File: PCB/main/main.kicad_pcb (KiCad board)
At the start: 2 copper layers, 121.9 x 91.4 mm, 53 parts, among them IC1 LM358DT, IC2 LM358DT, IC3 AT24C256C-SSHL-T, J1 Conn_01x33_Female, J2 Conn_01x33_Female, J3 Conn_01x33_Female, J4 Conn_01x33_Female, J5 47346-0001, J5 USB_B_Micro, Q1 IRF9540NPbF, U1 MCP73831-2-OT, U2 FT232RL, U3 MCP1700-3302E_TO92

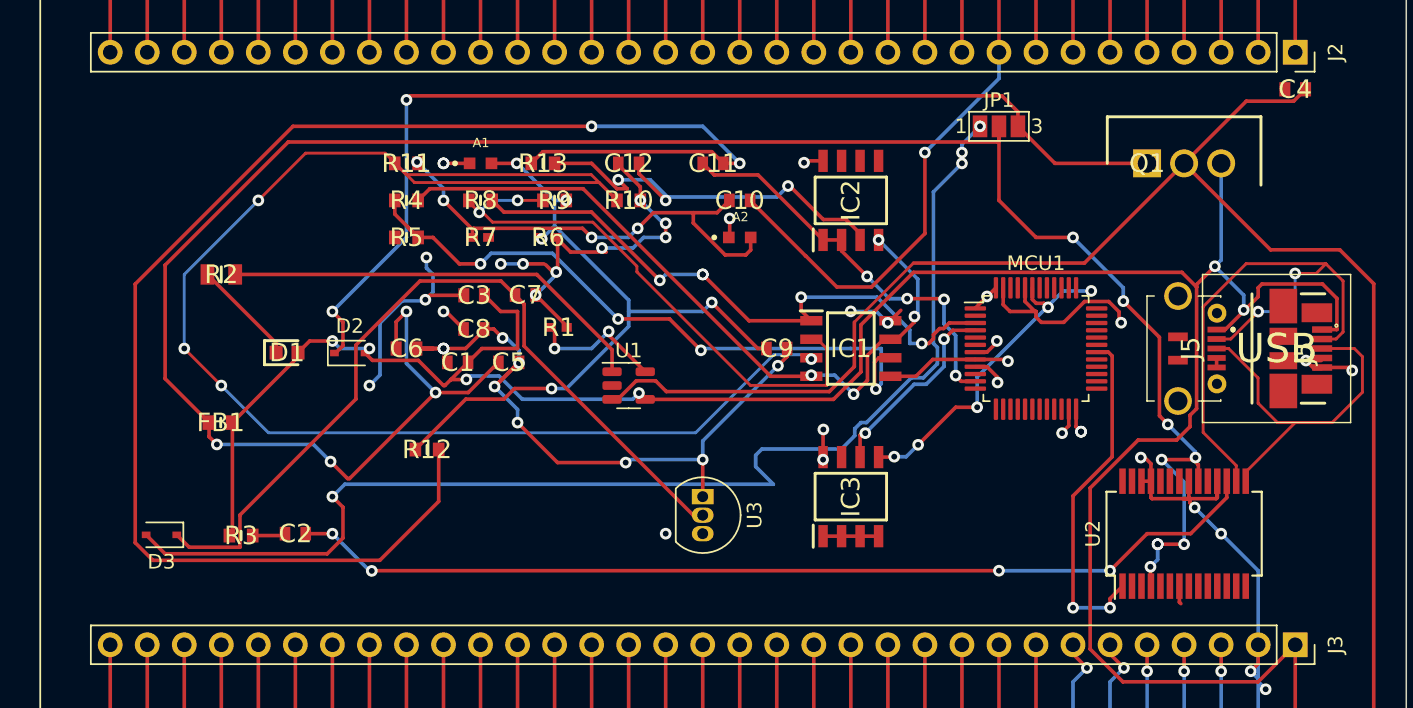
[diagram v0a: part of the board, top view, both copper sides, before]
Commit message: added more test points
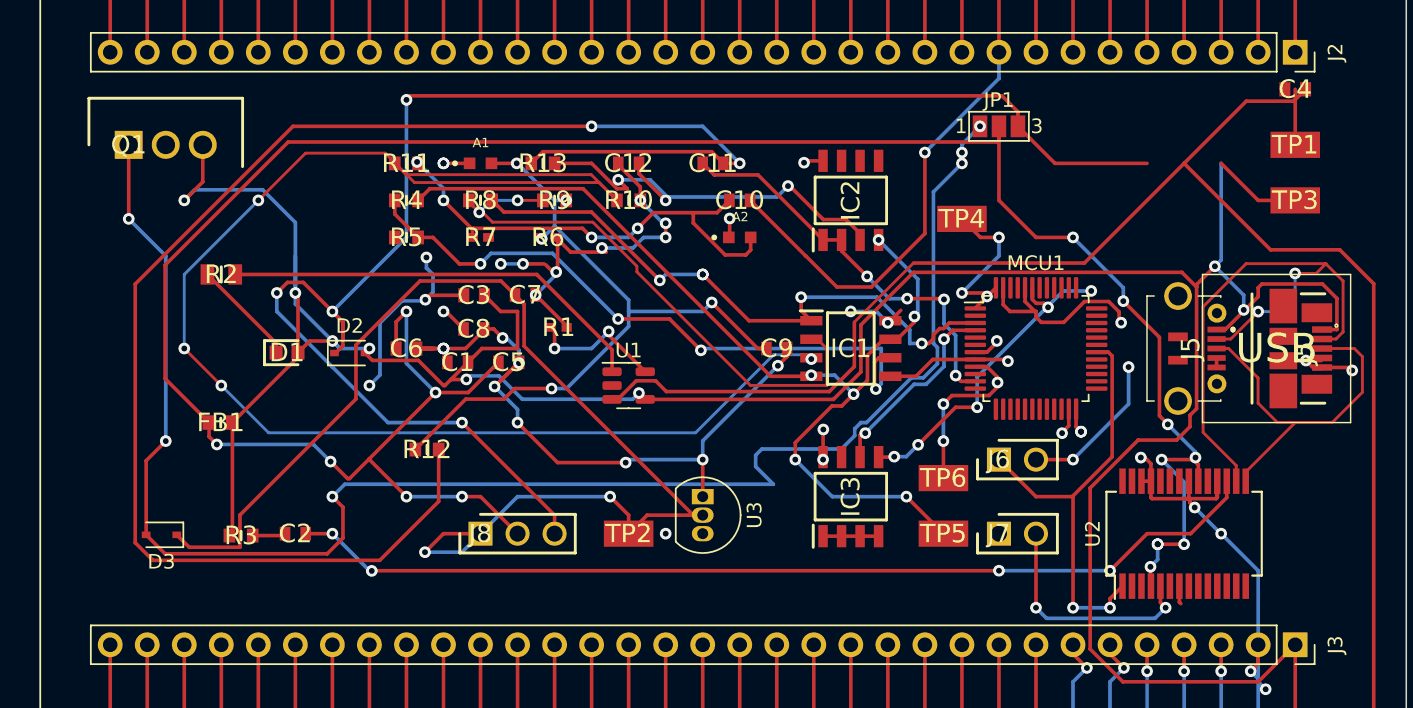
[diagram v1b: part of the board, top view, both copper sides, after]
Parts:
- added J6: PZ254V-11-02P, SamacSys_Parts:HDRV2W64P0X254_1X2_508X250X873P, F.Cu at (160.0, 104.1)
- added J7: PZ254V-11-02P, SamacSys_Parts:HDRV2W64P0X254_1X2_508X250X873P, F.Cu at (160.0, 109.2)
- added J8: MTP125-1103S1, SamacSys_Parts:HDRV3W64P0X254_1X3_762X250X885P, F.Cu at (124.5, 109.2)
- added TP1: 5017, SamacSys_Parts:5017, F.Cu at (180.3, 82.5)
- added TP2: 5017, SamacSys_Parts:5017, F.Cu at (134.6, 109.2)
- added TP3: 5017, SamacSys_Parts:5017, F.Cu at (180.3, 86.4)
- added TP4: 5017, SamacSys_Parts:5017, F.Cu at (157.5, 87.6)
- added TP5: 5017, SamacSys_Parts:5017, F.Cu at (156.2, 109.2)
- added TP6: 5017, SamacSys_Parts:5017, F.Cu at (156.2, 105.4)
- moved Q1 69.9 mm to (100.3, 82.5)
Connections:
- D3 pad 1: Net-(C7-Pad1) -> Net-(D2-Pad1)
- Q1 pad 1: Net-(D2-Pad1) -> Net-(D3-Pad2)
- U2 pad 1: USART1_TX -> Net-(J6-Pad1)
- U2 pad 5: USATR1_RX -> Net-(J7-Pad2)
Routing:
- net +5V: track 177.9 -> 213.8 mm, vias 6 -> 8
- net Net-(D2-Pad1): track 73.5 -> 107.9 mm, vias 2 -> 4
- net Net-(J6-Pad1): track 0.00 -> 30.1 mm, vias 0 -> 2
- net Net-(D3-Pad2): track 83.8 -> 112.1 mm, vias 4 -> 6
- net Net-(C7-Pad1): track 55.8 -> 83.1 mm, vias 0 -> 2
- net +3v3: track 20.9 -> 40.1 mm, vias 15 -> 19
- net -3v3: track 50.1 -> 68.9 mm, vias 4 -> 6
- net Net-(J7-Pad2): track 0.00 -> 16.2 mm, vias 0 -> 2
- net USART1_TX: track 23.9 -> 10.7 mm
- net VCC: track 153.4 -> 165.8 mm, vias 13 -> 15
- net Net-(BT1-Pad1): track 216.3 -> 220.1 mm

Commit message: pcb update
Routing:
- net Net-(BT1-Pad1): track 220.1 -> 272.0 mm, vias 0 -> 4
- net Net-(C7-Pad1): track 83.1 -> 48.1 mm
- net Net-(D2-Pad1): track 107.9 -> 124.0 mm, vias 4 -> 7
- net Net-(J6-Pad1): track 30.1 -> 17.3 mm
- net IN2-: track 45.9 -> 57.9 mm
- net GND: track 233.3 -> 244.3 mm, vias 31 -> 32
- net USART1_TX: track 10.7 -> 13.3 mm

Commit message: gerber files and dat
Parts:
- added C13: CC0603KRX7R9BB104, SamacSys_Parts:CAPC1608X90N, F.Cu at (99.1, 91.4)
- added J9: PZ254V-11-02P, SamacSys_Parts_Power:HDRV2W64P0X254_1X2_508X250X873P, F.Cu at (167.6, 81.3)
- added TP5: 5017, SamacSys_Parts_Power:5017, F.Cu at (144.8, 91.4)
- added TP6: 5017, SamacSys_Parts_Power:5017, B.Cu at (147.3, 81.3)
- added TP7: 5017, SamacSys_Parts_Power:5017, B.Cu at (162.6, 86.4)
- renumbered D3 to D2, D2 to D3, TP3 to TP1, TP1 to TP2, TP2 to TP3, TP5 to TP8, TP6 to TP9
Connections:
- D2 pad 2: Net-(D3-Pad2) -> (no net)
- MCU1 pad 7: +3v3 -> Net-(C13-Pad1)
- Q1 pad 1: Net-(D3-Pad2) -> Net-(D2-Pad2)
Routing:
- net Net-(D3-Pad2): track 112.1 -> 0.00 mm, vias 6 -> 0
- net Net-(D2-Pad2): track 0.00 -> 109.2 mm, vias 0 -> 4
- net GND: track 244.3 -> 295.9 mm, vias 32 -> 29
- net Vdiff: track 42.1 -> 73.5 mm
- net +3v3: track 40.1 -> 67.4 mm, vias 19 -> 17
- net Net-(C13-Pad1): track 0.00 -> 19.8 mm, vias 0 -> 2
- net Vout2: track 32.3 -> 43.7 mm, vias 4 -> 7
- net Net-(D2-Pad1): track 124.0 -> 114.5 mm
- net Vout1: track 47.5 -> 56.5 mm
- net Net-(BT1-Pad1): track 272.0 -> 271.2 mm
- net +5V: vias 8 -> 10

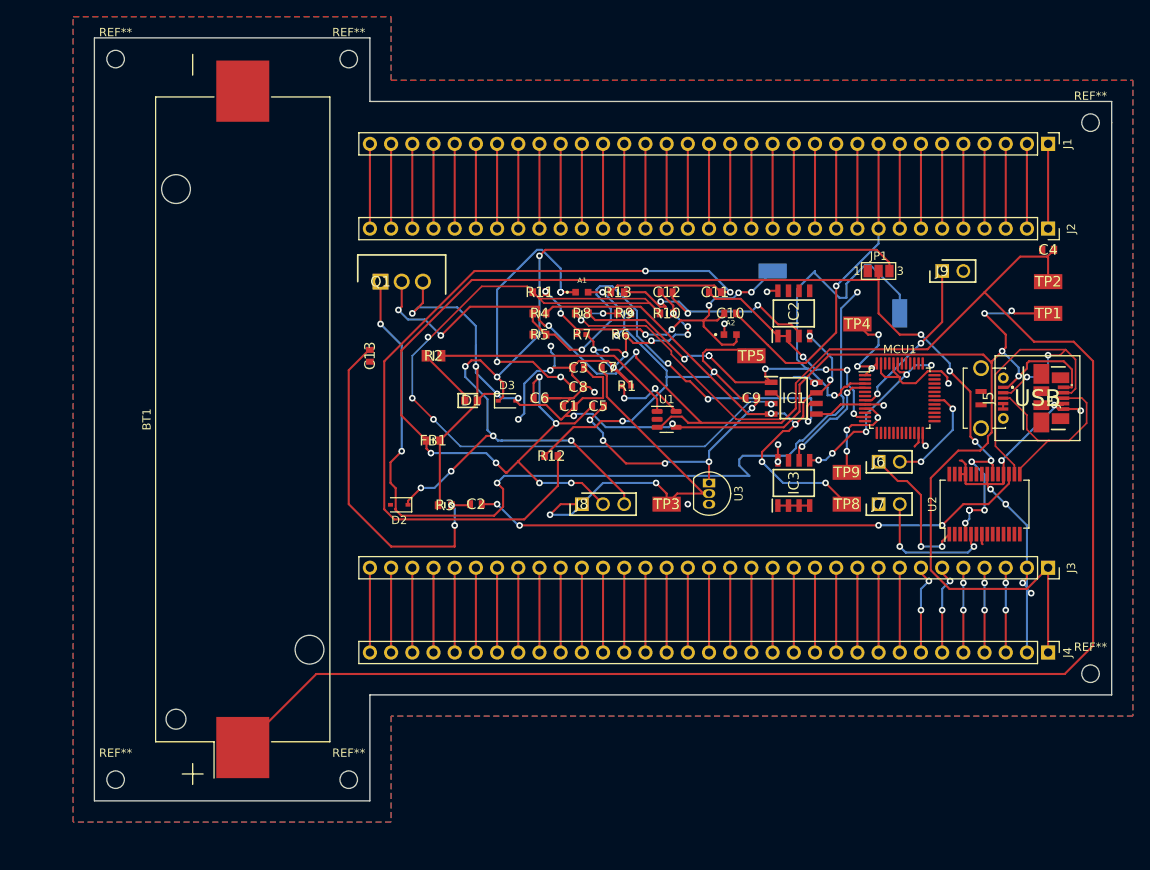
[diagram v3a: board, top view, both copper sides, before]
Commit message: modified power schematic
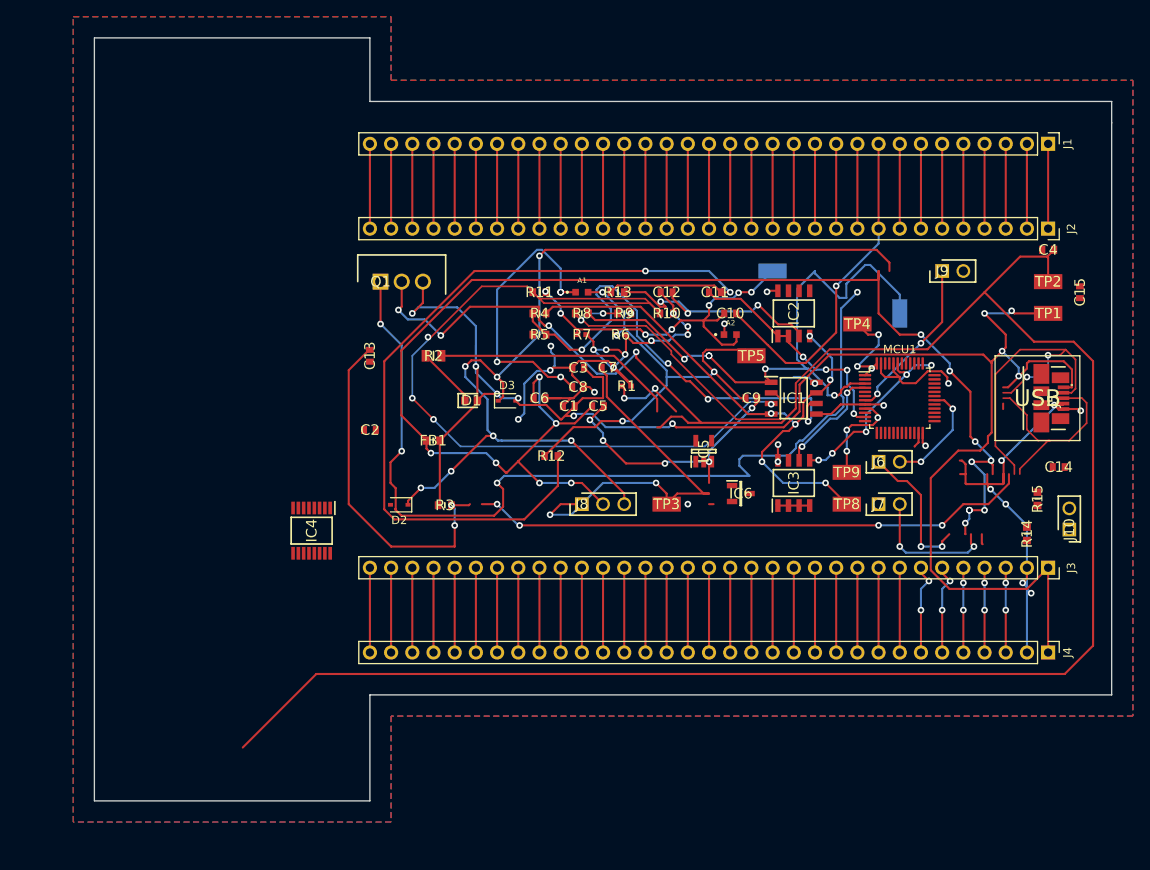
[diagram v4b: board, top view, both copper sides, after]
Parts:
- removed BT1: 3.7V, Battery:BatteryHolder_Keystone_1042_1x18650
- removed the J5 at (170.2, 96.5)
- removed JP1: Jumper_3_Open, Jumper:SolderJumper-3_P1.3mm_Open_Pad1.0x1.5mm_NumberLabels
- removed REF** (x6): MountingHole_2.1mm, MountingHole:MountingHole_2.1mm
- removed U1: MCP73831-2-OT, Package_TO_SOT_SMD:SOT-23-5
- removed U2: FT232RL, Package_SO:SSOP-28_5.3x10.2mm_P0.65mm
- removed U3: MCP1700-3302E_TO92, Package_TO_SOT_THT:TO-92_Inline
- added C14: CL10C470JB8NNNC, CAP1UF:CAPC1608X90N, F.Cu at (181.6, 104.8)
- added C15: CL10C470JB8NNNC, CAP1UF:CAPC1608X90N, F.Cu at (184.2, 83.8)
- added IC4: FT230XS-R, SamacSys_Parts:SOP64P599X175-16N, F.Cu at (92.1, 112.4)
- added IC5: MCP73831T-2ACI_OT, SamacSys_Parts:SOT95P270X145-5N, F.Cu at (139.1, 102.9)
- added IC6: MCP1700T-3302E_TT, SamacSys_Parts:SOT95P237X112-3N, F.Cu at (143.5, 108.0)
- added J10: PZ254V-11-02P, SamacSys_Parts:HDRV2W64P0X254_1X2_508X250X873P, F.Cu at (182.9, 112.3)
- added R14: 0603WAF270JT5E, R10K:RESC1608X55N, F.Cu at (177.8, 112.8)
- added R15: 0603WAF270JT5E, R10K:RESC1608X55N, F.Cu at (179.1, 108.6)
- C13: footprint SamacSys_Parts:CAPC1608X90N -> CAP1UF:CAPC1608X90N
- C2: value 100nF -> CC0603KRX7R9BB104; footprint SamacSys_Parts:CAPC1608X90N -> CAP1UF:CAPC1608X90N
- J9: footprint SamacSys_Parts_Power:HDRV2W64P0X254_1X2_508X250X873P -> SamacSys_Parts:HDRV2W64P0X254_1X2_508X250X873P
- TP5, TP6, TP7: footprint SamacSys_Parts_Power:5017 -> SamacSys_Parts:5017
- moved C2 15.5 mm to (99.1, 100.3)
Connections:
- C13 pad 1: (no net) -> Net-(C13-Pad1)
- C2 pad 1: GND -> /Power/3V3
- C2 pad 2: Net-(C2-Pad2) -> GND
- D2 pad 2: (no net) -> Net-(D2-Pad2)
- J6 pad 1: Net-(J6-Pad1) -> /Power/TXD
- J7 pad 2: Net-(J7-Pad2) -> /Power/RXD
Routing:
- net (no net): track 0.00 -> 68.1 mm, vias 0 -> 4
- net Net-(C2-Pad2): track 67.4 -> 0.00 mm, vias 4 -> 0
- net Net-(J6-Pad1): track 17.3 -> 0.00 mm, vias 2 -> 0
- net /Power/TXD: track 0.00 -> 17.3 mm, vias 0 -> 2
- net Net-(J7-Pad2): track 16.2 -> 0.00 mm, vias 2 -> 0
- net /Power/RXD: track 0.00 -> 16.2 mm, vias 0 -> 2
- net Earth: track 0.65 -> 0.00 mm

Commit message: new PCB
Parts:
- removed MCU1: STM32F030C8Tx, Package_QFP:LQFP-48_7x7mm_P0.5mm
- C13, C14, C15, C2: footprint CAP1UF:CAPC1608X90N -> SamacSys_Parts:CAPC1608X90N
- IC4: footprint SamacSys_Parts:SOP64P599X175-16N -> SamacSys_Parts_Power:SOP64P599X175-16N
- IC5: footprint SamacSys_Parts:SOT95P270X145-5N -> SamacSys_Parts_Power:SOT95P270X145-5N
- IC6: footprint SamacSys_Parts:SOT95P237X112-3N -> SamacSys_Parts_Power:SOT95P237X112-3N
- J10, J6, J7, J9: footprint SamacSys_Parts:HDRV2W64P0X254_1X2_508X250X873P -> SamacSys_Parts_Power:HDRV2W64P0X254_1X2_508X250X873P
- J5: footprint SamacSys_Parts_Power:47346-0001 -> SamacSys_Parts_Microcontroller:47346-0001
- J8: footprint SamacSys_Parts:HDRV3W64P0X254_1X3_762X250X885P -> SamacSys_Parts_Power:HDRV3W64P0X254_1X3_762X250X885P
- R14, R15: footprint R10K:RESC1608X55N -> SamacSys_Parts:RESC1608X55N
- TP1, TP2, TP3, TP4, TP5, TP8, TP9: footprint SamacSys_Parts:5017 -> SamacSys_Parts_Power:5017
- TP6, TP7: footprint SamacSys_Parts:5017 -> SamacSys_Parts_Power:5017; moved to F.Cu
- moved J10 82.4 mm to (101.6, 98.7), turned to 180 degrees
- moved R4 70.6 mm to (179.6, 123.2), turned to 90 degrees
- moved C13 67.1 mm to (164.1, 107.7), turned to 0 degrees
- moved TP6 65.3 mm to (105.0, 131.0), turned to 0 degrees
- moved R7 63.4 mm to (172.6, 130.2), turned to 180 degrees
- moved R11 63.4 mm to (172.6, 118.2)
- moved J6 61.7 mm to (98.6, 109.7)
- moved R5 58.4 mm to (161.7, 129.2)
- moved A2 58.0 mm to (99.6, 128.2)
- moved TP1 55.6 mm to (131.1, 112.2), turned to -90 degrees
- moved Q1 54.7 mm to (131.2, 127.7), turned to 180 degrees
- moved R9 54.0 mm to (167.1, 125.2)
- moved TP2 52.4 mm to (131.0, 100.3)
- moved C4 52.0 mm to (140.1, 111.7), turned to -90 degrees
- moved C15 49.1 mm to (145.6, 114.2), turned to 90 degrees
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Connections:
- net Net-(C13-Pad1) renamed /microcontroller_interfacing/NRST
- net USATR1_RX renamed /Power/PA10
- IC3 pad 5: /microcontroller_interfacing/SDA_P43 -> /microcontroller_interfacing/PB7
- IC3 pad 6: /microcontroller_interfacing/SCL_P4 -> /microcontroller_interfacing/PC15
- J6 pad 2: USART1_TX -> /Power/PA9
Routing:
- net Net-(C4-Pad2): track 271.2 -> 79.9 mm, vias 4 -> 2
- net Net-(D2-Pad2): track 109.2 -> 8.55 mm, vias 4 -> 0
- net VCC: track 165.8 -> 75.1 mm, vias 15 -> 0
- net Net-(C11-Pad2): track 106.2 -> 18.9 mm, vias 2 -> 0
- net IN1+: track 103.8 -> 17.8 mm, vias 4 -> 3
- net Net-(D2-Pad1): track 114.5 -> 54.4 mm, vias 7 -> 4
- net Net-(IC4-Pad8): track 0.00 -> 49.2 mm, vias 0 -> 2
- net Vdiff: track 73.5 -> 25.6 mm, vias 5 -> 2
- net GND: track 295.9 -> 248.9 mm, vias 29 -> 40
- net Vout2: track 43.7 -> 89.0 mm, vias 7 -> 2
- net +3v3: track 67.4 -> 110.4 mm, vias 17 -> 8
- net Vout1: track 56.5 -> 94.9 mm, vias 5 -> 6
- net (no net): track 68.1 -> 31.6 mm, vias 4 -> 7
- net +5V: track 213.8 -> 180.9 mm
- net Net-(IC4-Pad9): track 0.00 -> 31.6 mm, vias 0 -> 4
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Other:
- board size 121.9 x 91.4 mm -> 97 x 73 mm

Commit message: generated Gerbers
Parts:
- added REF**: MountingHole_2.1mm, MountingHole:MountingHole_2.1mm, F.Cu at (185.9, 82.8)
- added REF**: MountingHole_2.1mm, MountingHole:MountingHole_2.1mm, F.Cu at (186.4, 146.8)
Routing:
- net GND: track 248.9 -> 244.5 mm
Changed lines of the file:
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@@
       (layerselection 0x00010fc_ffffffff)
       (disableapertmacros false)
-      (usegerberextensions false)
-      (usegerberattributes true)
-      (usegerberadvancedattributes true)
-      (creategerberjobfile true)
+      (usegerberextensions true)
+      (usegerberattributes false)
+      (usegerberadvancedattributes false)
+      (creategerberjobfile false)
       (svguseinch false)
       (svgprecision 6)
@@
       (psa4output false)
       (plotreference true)
-      (plotvalue true)
+      (plotvalue false)
       (plotinvisibletext false)
       (sketchpadsonfab false)
-      (subtractmaskfromsilk false)
+      (subtractmaskfromsilk true)
       (outputformat 1)
       (mirror false)
-      (drillshape 1)
+      (drillshape 0)
       (scaleselection 1)
-      (outputdirectory "")
+      (outputdirectory "Gerbers/")
     )
   )
@@
     )
   )
+  (footprint "MountingHole:MountingHole_2.1mm" (layer "F.Cu")
+    (at 185.928 82.804)
+    (descr "Mounting Hole 2.1mm, no annular")
+    (tags "mounting hole 2.1mm no annular")
+    (attr exclude_from_pos_files exclude_from_bom)
+    (fp_text reference "REF**" (at 0 -3.2) (layer "F.SilkS")
+      (effects (font (size 1 1) (thickness 0.15)))
+    )
+    (fp_text value "MountingHole_2.1mm" (at 0 3.2) (layer "F.Fab")
+      (effects (font (size 1 1) (thickness 0.15)))
+    )
+    (fp_text user "${REFERENCE}" (at 0 0) (layer "F.Fab")
+      (effects (font (size 1 1) (thickness 0.15)))
+    )
+    (fp_circle (center 0 0) (end 2.1 0) (layer "Cmts.User") (width 0.15) (fill none))
+    (fp_circle (center 0 0) (end 2.35 0) (layer "F.CrtYd") (width 0.05) (fill none))
+    (pad "" np_thru_hole circle (at 0 0) (size 2.1 2.1) (drill 2.1) (layers *.Cu *.Mask))
+  )
   (footprint "SamacSys_Parts:RESC1005X37N" (layer "F.Cu")
     (at 152.82 129.705)
@@
     )
   )
+  (footprint "MountingHole:MountingHole_2.1mm" (layer "F.Cu")
+    (at 186.436 146.812)
+    (descr "Mounting Hole 2.1mm, no annular")
+    (tags "mounting hole 2.1mm no annular")
+    (attr exclude_from_pos_files exclude_from_bom)
+    (fp_text reference "REF**" (at 0 -3.2) (layer "F.SilkS")
+      (effects (font (size 1 1) (thickness 0.15)))
+    )
+    (fp_text value "MountingHole_2.1mm" (at 0 3.2) (layer "F.Fab")
+      (effects (font (size 1 1) (thickness 0.15)))
+    )
+    (fp_text user "${REFERENCE}" (at 0 0) (layer "F.Fab")
+      (effects (font (size 1 1) (thickness 0.15)))
+    )
+    (fp_circle (center 0 0) (end 2.1 0) (layer "Cmts.User") (width 0.15) (fill none))
+    (fp_circle (center 0 0) (end 2.35 0) (layer "F.CrtYd") (width 0.05) (fill none))
+    (pad "" np_thru_hole circle (at 0 0) (size 2.1 2.1) (drill 2.1) (layers *.Cu *.Mask))
+  )
   (footprint "SamacSys_Parts:RESC1608X55N" (layer "F.Cu")
     (at 168.62 109.705 90)
@@
   (segment (start 145 111) (end 145.975402 111) (width 0.25) (layer "F.Cu") (net 2))
   (segment (start 177.4 134.64) (end 177.4 132.4) (width 0.25) (layer "F.Cu") (net 2))
-  (segment (start 183 108) (end 184 107) (width 0.25) (layer "F.Cu") (net 2))
   (segment (start 164.83 107.705) (end 164.83 108.17) (width 0.25) (layer "F.Cu") (net 2))
   (segment (start 99.08 94.42) (end 98.66 94) (width 0.25) (layer "F.Cu") (net 2))
@@
   (segment (start 163.10952 131.44952) (end 167.55048 131.44952) (width 0.25) (layer "F.Cu") (net 2))
   (segment (start 114.302 123.302) (end 114.302 124.493) (width 0.25) (layer "F.Cu") (net 2))
-  (segment (start 183 109.7125) (end 183 108) (width 0.25) (layer "F.Cu") (net 2))
   (segment (start 145.975402 111) (end 145.987701 111.012299) (width 0.25) (layer "F.Cu") (net 2))
   (segment (start 172.33 125.705) (end 172.33 126.9705) (width 0.25) (layer "F.Cu") (net 2))
@@
   (segment (start 98.66 134.64) (end 98.66 144.8) (width 0.25) (layer "F.Cu") (net 2))
   (segment (start 152 102.024598) (end 152 103) (width 0.25) (layer "F.Cu") (net 2))
-  (segment (start 183.9 110.6125) (end 183 109.7125) (width 0.25) (layer "F.Cu") (net 2))
   (segment (start 99 101) (end 99 98.785) (width 0.25) (layer "F.Cu") (net 2))
   (segment (start 167.55048 131.44952) (end 168 131) (width 0.25) (layer "F.Cu") (net 2))
